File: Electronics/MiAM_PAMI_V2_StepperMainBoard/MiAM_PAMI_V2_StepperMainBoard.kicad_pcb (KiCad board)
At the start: 2 copper layers, 64 x 95 mm, 31 parts, among them J1 Conn_01x11_Male, J2 Conn_01x03_Male, J3 Conn_01x03_Male, U1 ESP32-DEVKITC-32U, U2 3V3, U3 MT3608, U4 LM7805_TO220

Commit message: Fix pcb & add driver board
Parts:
- moved MS3 13.4 mm to (122.6, 49.0), turned to -90 degrees
- moved MS2 8.43 mm to (126.1, 49.0), turned to -90 degrees
- moved C3 7.82 mm to (128.8, 57.4)
- moved MS1 3.50 mm to (129.7, 49.0), turned to -90 degrees
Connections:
- J1 pad 10: +3V3 -> /NOT_MOT_EN
- J1 pad 11: GND -> +3V3
- J1 pad 2: /MS1 -> GND
- J1 pad 3: /MS2 -> /MS1
- J1 pad 4: /MS3 -> /MS2
- J1 pad 5: /STEP_1 -> /MS3
- J1 pad 6: /DIR_1 -> /STEP_1
- J1 pad 7: /STEP_2 -> /DIR_1
- J1 pad 8: /DIR_2 -> /STEP_2
- J1 pad 9: /NOT_MOT_EN -> /DIR_2
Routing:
- net /EMERGENCY_BUTTON: track 150.6 -> 145.9 mm
- net /MS3: track 24.6 -> 27.6 mm, vias 1 -> 0
- net +3V3: track 198.3 -> 201.2 mm, vias 4 -> 8
- net /DIR_2: track 37.4 -> 38.8 mm
- net /NOT_MOT_EN: track 35.2 -> 36.3 mm
- net /DIR_1: track 33.3 -> 32.2 mm
- net /STEP_1: track 26.5 -> 25.4 mm
- net /MS2: track 22.0 -> 21.1 mm, vias 1 -> 0
- net /MS1: track 14.5 -> 14.6 mm, vias 1 -> 0
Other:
- board text added: "MiAM PAMI Stepper board 11/2023"

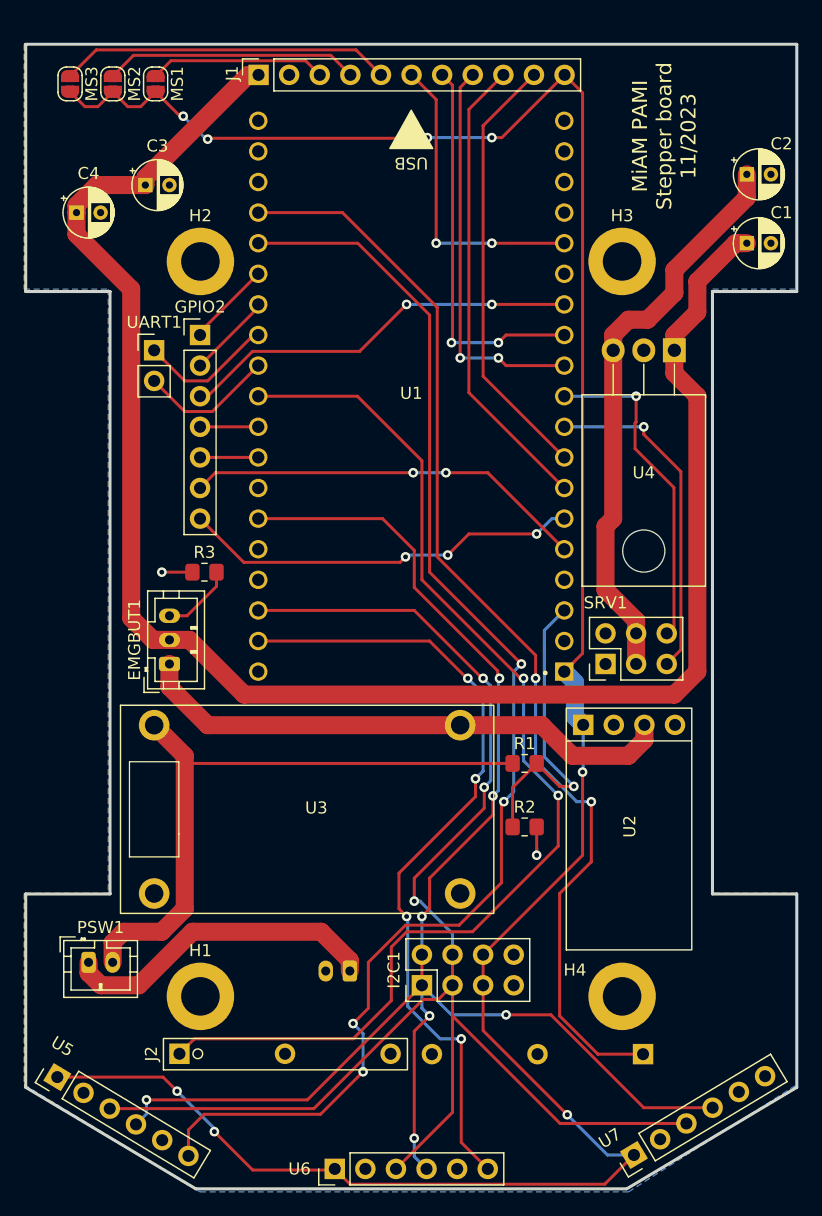
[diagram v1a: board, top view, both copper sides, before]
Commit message: Put stepper driver on main board
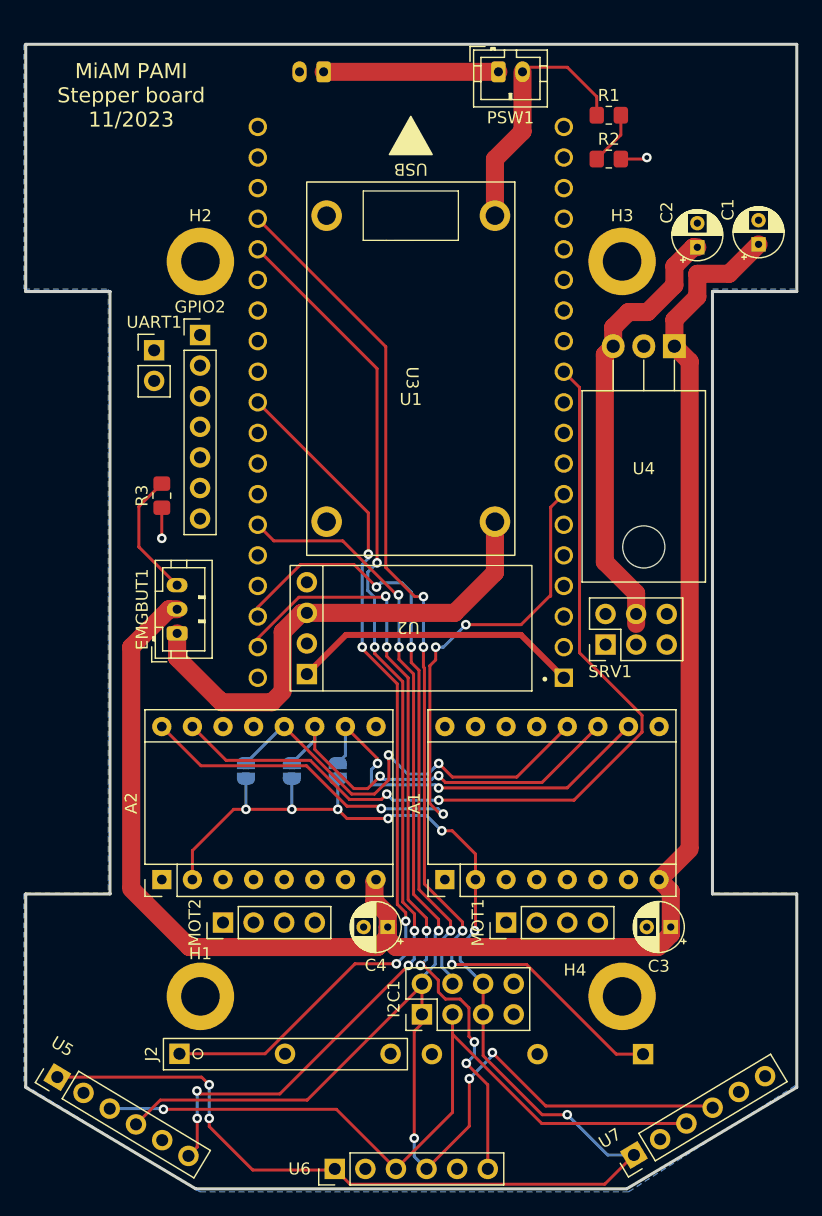
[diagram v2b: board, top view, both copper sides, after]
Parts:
- removed J1: Conn_01x11_Male, Connector_PinSocket_2.54mm:PinSocket_1x11_P2.54mm_Vertical
- added A1: Pololu_Breakout_A4988, Module:Pololu_Breakout-16_15.2x20.3mm, F.Cu at (153.7, 115.1)
- added A2: Pololu_Breakout_A4988, Module:Pololu_Breakout-16_15.2x20.3mm, F.Cu at (130.2, 115.1)
- added MOT1: Conn_01x04_Male, Connector_PinHeader_2.54mm:PinHeader_1x04_P2.54mm_Vertical, F.Cu at (158.8, 118.6)
- added MOT2: Conn_01x04_Male, Connector_PinHeader_2.54mm:PinHeader_1x04_P2.54mm_Vertical, F.Cu at (135.3, 118.6)
- MS1, MS2, MS3: moved to B.Cu
- moved PSW1 81.4 mm to (158.1, 48.0)
- moved C3 75.5 mm to (172.4, 119.0), turned to 180 degrees
- moved BAT1 74.7 mm to (143.6, 48.0)
- moved C4 64.7 mm to (148.9, 119.0), turned to 180 degrees
- moved MS1 59.0 mm to (144.8, 106.0)
- moved MS2 58.9 mm to (141.0, 106.0)
- moved MS3 58.9 mm to (137.2, 106.0)
- moved R2 55.9 mm to (167.3, 55.2)
- moved R1 54.3 mm to (167.3, 51.6)
- moved U3 37.6 mm to (150.8, 72.6), turned to -90 degrees
- moved U2 24.5 mm to (151.1, 94.2), turned to 180 degrees
- moved C2 7.31 mm to (174.6, 62.6), turned to 90 degrees
- moved R3 7.27 mm to (130.2, 83.2), turned to 90 degrees
- moved EMGBUT1 2.62 mm to (131.4, 94.6)
- moved I2C1 2.41 mm to (151.8, 126.2)
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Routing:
- net +3V3: track 201.2 -> 149.3 mm, vias 8 -> 9
- net /STEP_2: track 32.8 -> 75.2 mm
- net /NOT_MOT_EN: track 36.3 -> 0.00 mm
- net /POWER_SWITCH: track 56.1 -> 21.8 mm
- net /GPIO12: track 33.4 -> 0.00 mm, vias 2 -> 0
- net /GPIO34: track 33.4 -> 0.00 mm, vias 2 -> 0
- net /GPIO35: track 33.2 -> 0.00 mm, vias 3 -> 0
- net /DIR_1: track 32.2 -> 0.00 mm, vias 2 -> 0
- net /SERVO_PWM_1: track 28.0 -> 0.00 mm, vias 1 -> 0
- net /SERVO_PWM_2: track 27.3 -> 0.00 mm, vias 1 -> 0
- net /STEP_1: track 25.4 -> 0.00 mm, vias 2 -> 0
- net /DIR_2: track 38.8 -> 61.7 mm, vias 0 -> 4
- net /BAT_READING: track 26.3 -> 4.46 mm, vias 1 -> 0
- net /GPIO5: track 93.8 -> 73.5 mm, vias 2 -> 4
- net /MS1: track 14.6 -> 33.0 mm, vias 0 -> 2
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
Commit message: Initial commit PAMI V3
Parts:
- removed C1: 0.22uF, Capacitor_THT:CP_Radial_D4.0mm_P2.00mm
- removed C2: 0.1uF, Capacitor_THT:CP_Radial_D4.0mm_P2.00mm
- removed PSW1: Conn_01x02_Female, Connector_JST:JST_PH_B2B-PH-K_1x02_P2.00mm_Vertical
- added SW1: SW_DPDT_x2, MiAM_ESP32_Footprints:SS-12D11, F.Cu at (150.9, 55.0)
- BAT1: moved to F.Cu
- U4: value LM7805_TO220 -> 3V3; footprint Package_TO_SOT_THT:TO-220-3_Horizontal_TabDown -> MiAM_ESP32_Footprints:VoltageRegulator
- moved BAT1 14.1 mm to (132.2, 56.2), turned to 90 degrees
- moved U4 9.76 mm to (170.4, 80.3), turned to 90 degrees
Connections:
- U4 pad 1: /EMERGENCY_BUTTON -> /5V_POWER
- U4 pad 3: /5V_POWER -> /EMERGENCY_BUTTON
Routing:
- net /BATTERY_INPUT: track 14.5 -> 28.1 mm
- net /EMERGENCY_BUTTON: track 141.5 -> 129.4 mm
- net /5V_POWER: track 36.6 -> 25.4 mm
- net /POWER_SWITCH: track 21.8 -> 24.5 mm
